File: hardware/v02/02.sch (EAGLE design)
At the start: 29 parts, among them IC1 MSP430G2553, IC2 78L05Z, X2 RJ45-6L-B

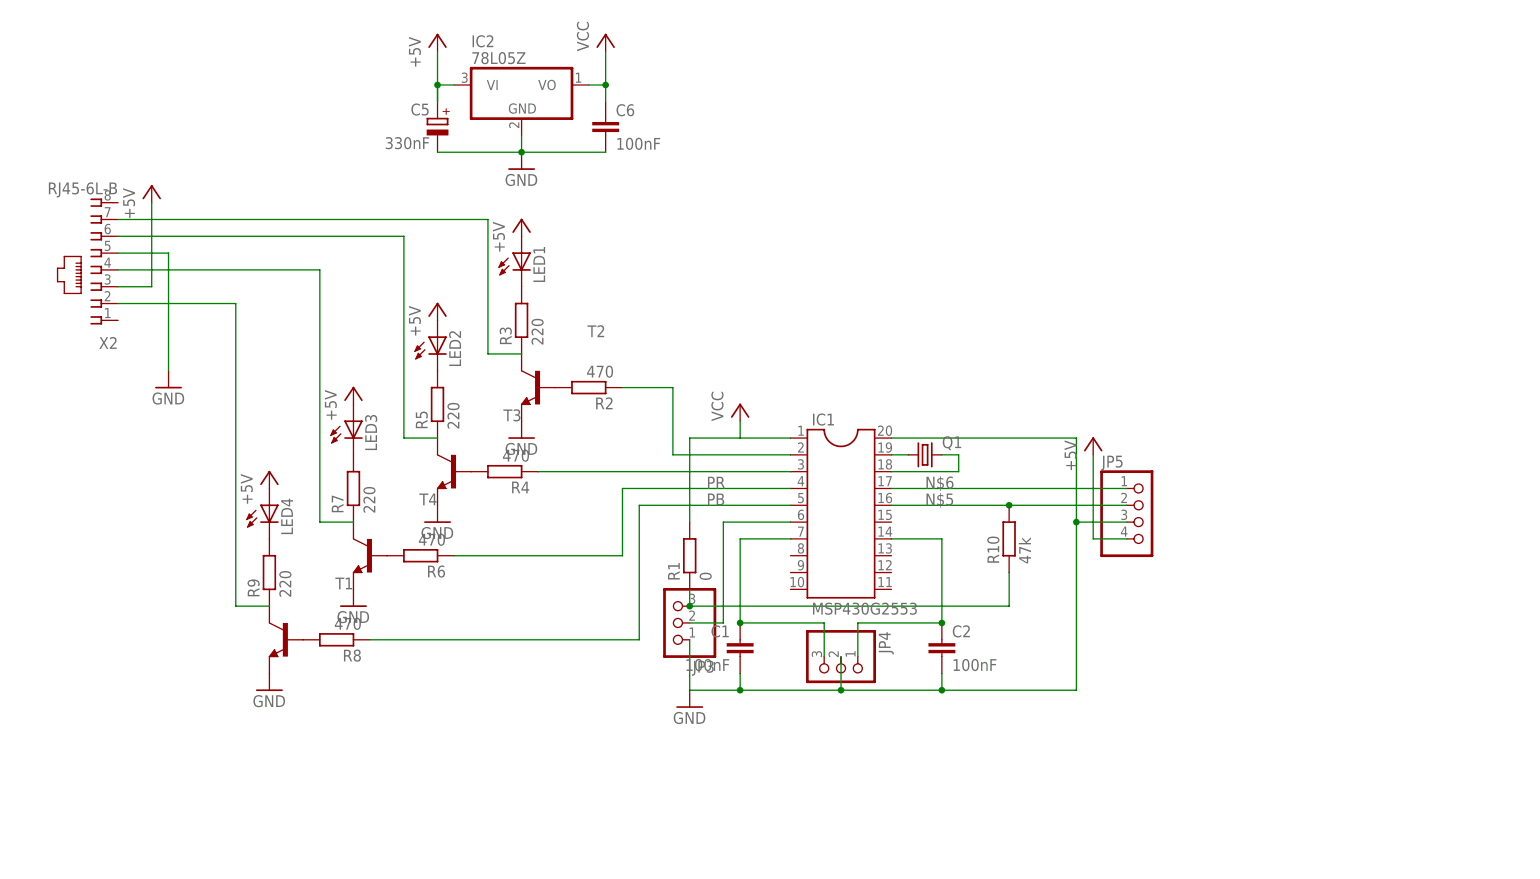
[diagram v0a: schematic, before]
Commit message: remove/rename some files
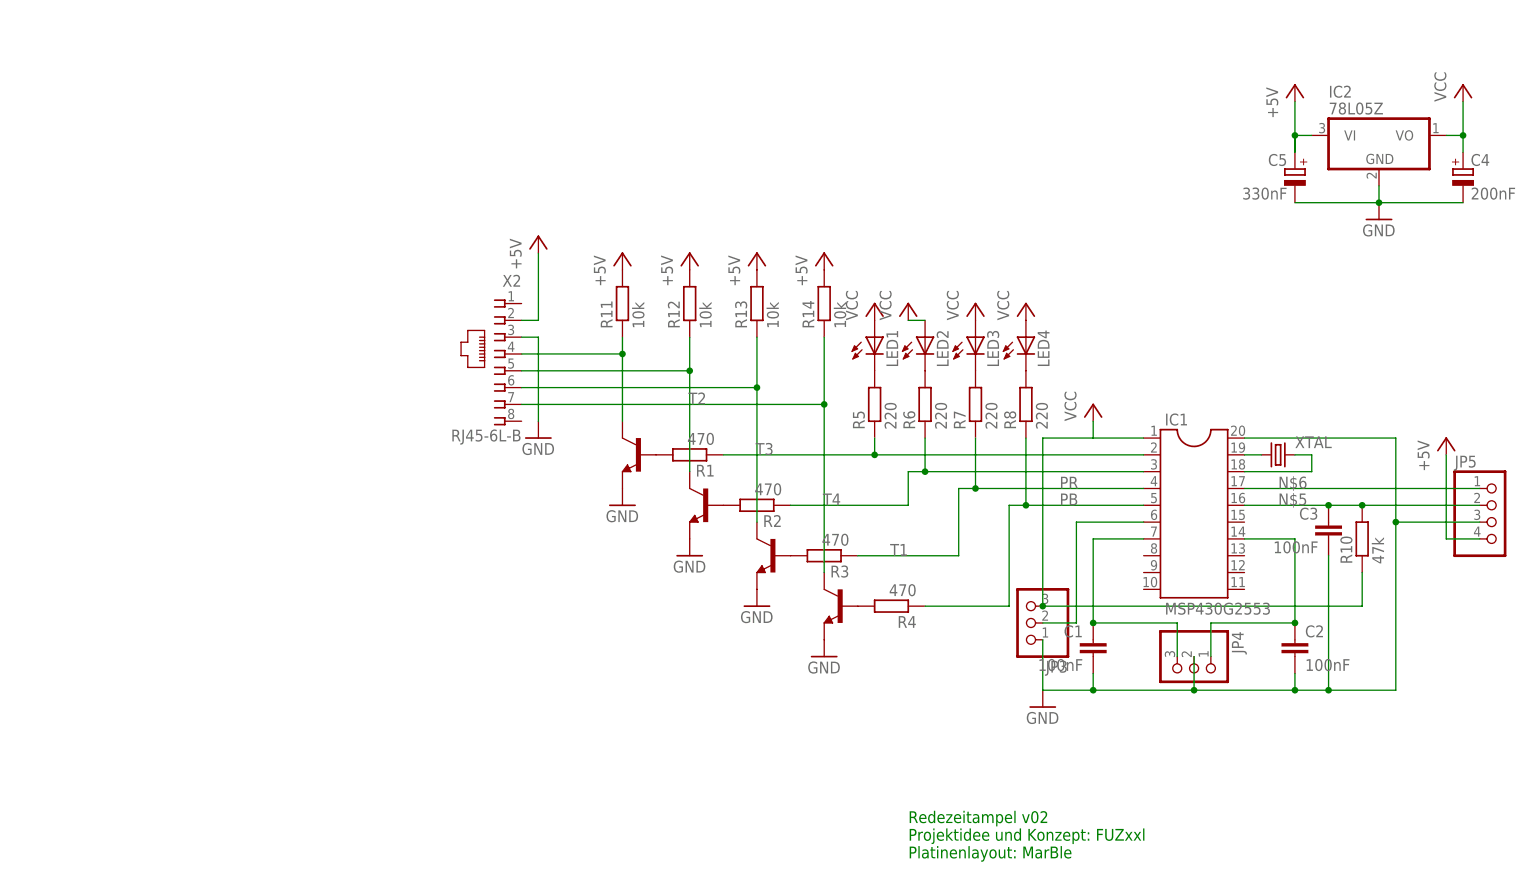
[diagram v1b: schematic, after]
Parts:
- removed C6: 100nF, rcl:C-EU025-024X044
- removed Q1: (no value), crystal:CRYSTALTC26H
- removed R9: 220, rcl:R-EU_0207/10
- added C3: 100nF, rcl:C-EU025-024X044
- added C4: 200nF, rcl:CPOL-EUB45181A
- added R11, R12, R13, R14: 10k, rcl:R-EU_0207/10
- added XTAL: (no value), crystal:CRYSTALTC26H
- R1: value 0 -> 470; device rcl:R-EU_0207/12 -> rcl:R-EU_0207/10
- R3: value 220 -> 470
- R6, R8: value 470 -> 220
- T1, T2, T3, T4: device transistor:-NPN-TO92 -> transistor:-NPN-TO92-EBC
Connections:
- removed net N$10: R9.1, T1.C, X2.2
- removed net N$14: R3.1, T2.C, X2.7
- removed net N$15: JP3.3, R1.1, R10.1
- removed net N$19: R5.1, T3.C, X2.6
- removed net N$22: R7.1, T4.C, X2.4
- new net N$27: R14.1, T1.C, X2.7
- new net N$28: R13.1, T4.C, X2.6
- new net N$29: R12.1, T3.C, X2.5
- new net N$30: R11.1, T2.C, X2.4
- net +5V: now also R11.2, R12.2, R13.2, R14.2, X2.2; no longer LED1.A, LED2.A, LED3.A, LED4.A, X2.3
- net GND: now also C3.2, C4.-, X2.3; no longer C6.2, X2.5
- net N$11: now also R4.2; no longer R8.2
- net N$12: now also R1.1, R5.1; no longer R2.1
- net N$13: now also R5.2; no longer R3.2
- net N$16: now also R1.2; no longer R2.2
- net N$17: now also R6.2; no longer R5.2
- net N$2: now also XTAL.1; no longer Q1.1
- net N$20: now also R2.2; no longer R4.2
- net N$23: now also R3.2; no longer R6.2
- net N$5: now also C3.1
- net N$7: now also XTAL.2; no longer Q1.2
- net N$8: now also R8.2; no longer R9.2
- net N$9: now also R2.1, R6.1; no longer R4.1
- net PB: now also R4.1
- net PR: now also R3.1, R7.1; no longer R6.1
- net VCC: now also C4.+, JP3.3, LED1.A, LED2.A, LED3.A, LED4.A, R10.1; no longer C6.1, R1.2
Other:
- note added: "Redezeitampel v02 Projektidee und Konzept: FUZxxl Platinenlayout: MarBle"
- moved on the sheet: C1, C2, C5, IC1, IC2, JP3, JP4, JP5, LED1, LED2, LED3, LED4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

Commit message: avoid one wire bridge
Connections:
- net N$27 renamed OUT4
- net N$28 renamed OUT3
- net N$29 renamed OUT2
- net N$30 renamed OUT1
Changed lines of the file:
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@@
 <?xml version="1.0" encoding="utf-8"?>
 <!DOCTYPE eagle SYSTEM "eagle.dtd">
-<eagle version="6.6.0">
+<eagle version="6.5.0">
 <drawing>
 <settings>
@@
 </segment>
 </net>
-<net name="N$27" class="0">
+<net name="OUT4" class="0">
 <segment>
 <pinref part="T1" gate="G$1" pin="C"/>
@@
 </segment>
 </net>
-<net name="N$28" class="0">
+<net name="OUT3" class="0">
 <segment>
 <pinref part="T4" gate="G$1" pin="C"/>
@@
 </segment>
 </net>
-<net name="N$29" class="0">
+<net name="OUT2" class="0">
 <segment>
 <pinref part="T3" gate="G$1" pin="C"/>
@@
 </segment>
 </net>
-<net name="N$30" class="0">
+<net name="OUT1" class="0">
 <segment>
 <pinref part="T2" gate="G$1" pin="C"/>
